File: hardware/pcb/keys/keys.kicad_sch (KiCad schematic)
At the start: 28 parts, among them J1 Conn_02x08_Odd_Even, J2 Conn_02x08_Odd_Even, SW1 SW_SPST, SW11 SW_SPST, SW12 SW_SPST, SW17 SW_SPST, SW18 SW_SPST, SW2 SW_SPST, SW23 SW_SPST, SW24 SW_SPST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

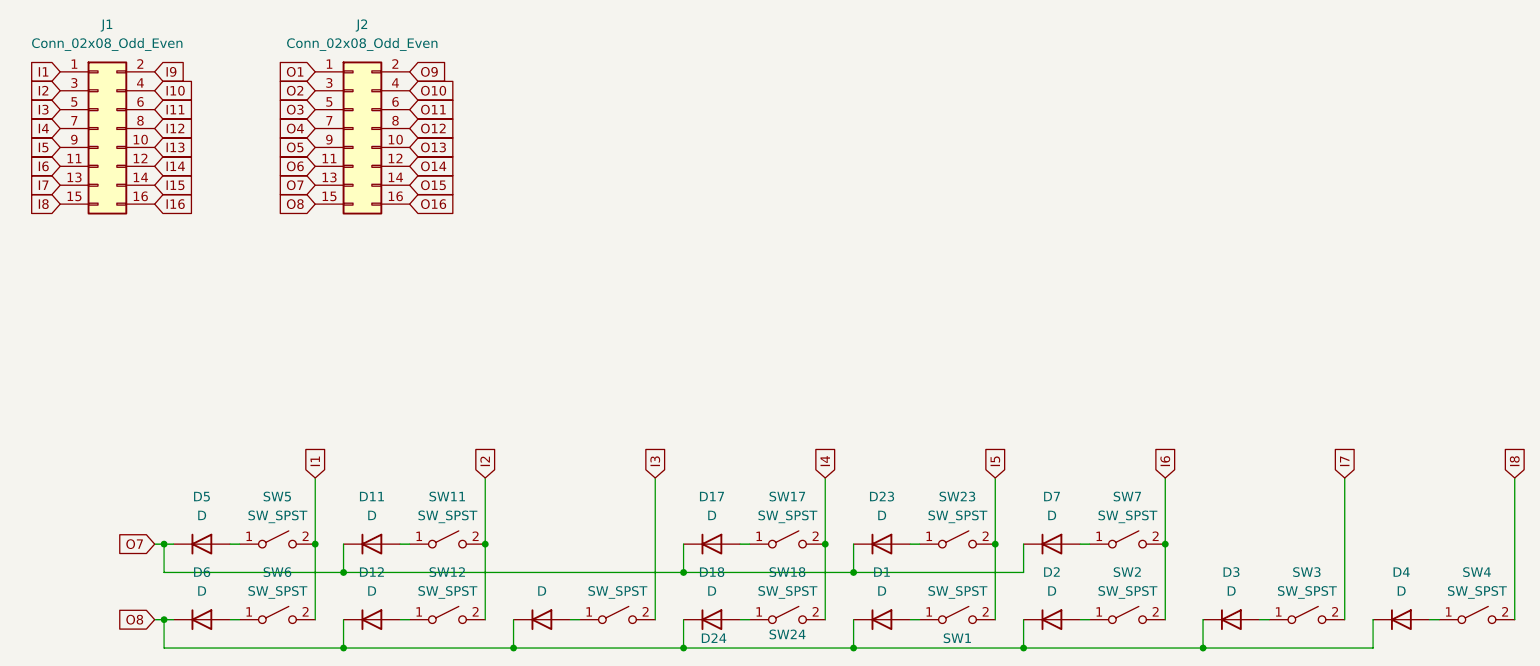
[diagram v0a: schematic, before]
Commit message: hardware: add schematics
add controls, io, keys, and nucleo hat boards
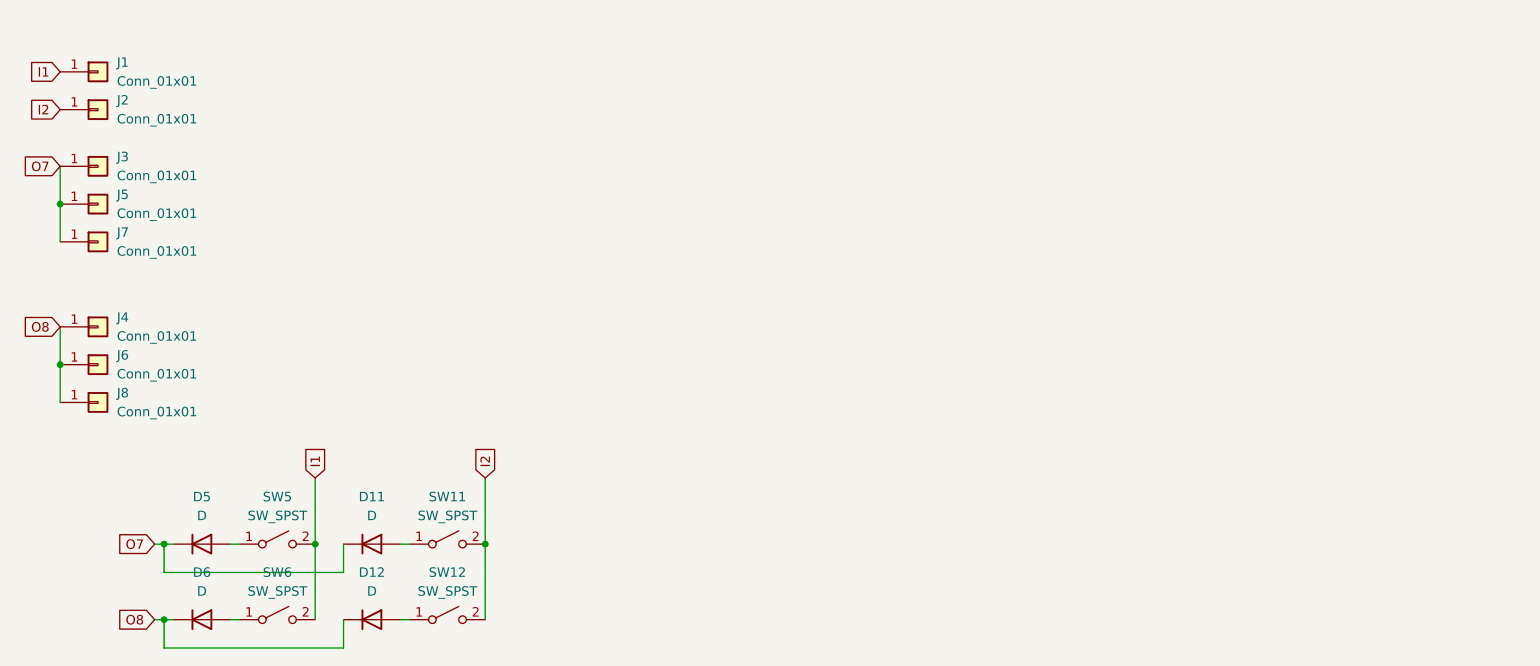
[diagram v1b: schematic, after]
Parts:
- removed D1, D17, D18, D2, D23, D24, D3, D4, D7: D, Diode_THT:D_DO-35_SOD27_P7.62mm_Horizontal, symbol Device:D
- removed J1, J2: Conn_02x08_Odd_Even, Connector_PinHeader_1.27mm:PinHeader_2x08_P1.27mm_Vertical, symbol Connector_Generic:Conn_02x08_Odd_Even
- removed SW1, SW17, SW18, SW2, SW23, SW24, SW3, SW4, SW7: SW_SPST, Button_Switch_Keyboard:SW_Cherry_MX_1.00u_PCB, symbol Switch:SW_SPST
- added J1, J2, J3, J4, J5, J6, J7, J8: Conn_01x01, Connector_PinHeader_1.27mm:PinHeader_1x01_P1.27mm_Vertical, symbol Connector_Generic:Conn_01x01
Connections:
- net I1: now also J1.1 (Pin_1)
- net I2: now also J2.1 (Pin_1)
- net O7: now also J3.1 (Pin_1), J5.1 (Pin_1), J7.1 (Pin_1)
- net O8: now also J4.1 (Pin_1), J6.1 (Pin_1), J8.1 (Pin_1)
